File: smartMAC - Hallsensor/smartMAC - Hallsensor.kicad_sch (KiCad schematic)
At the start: 6 parts, among them J1 Conn_01x03_Pin

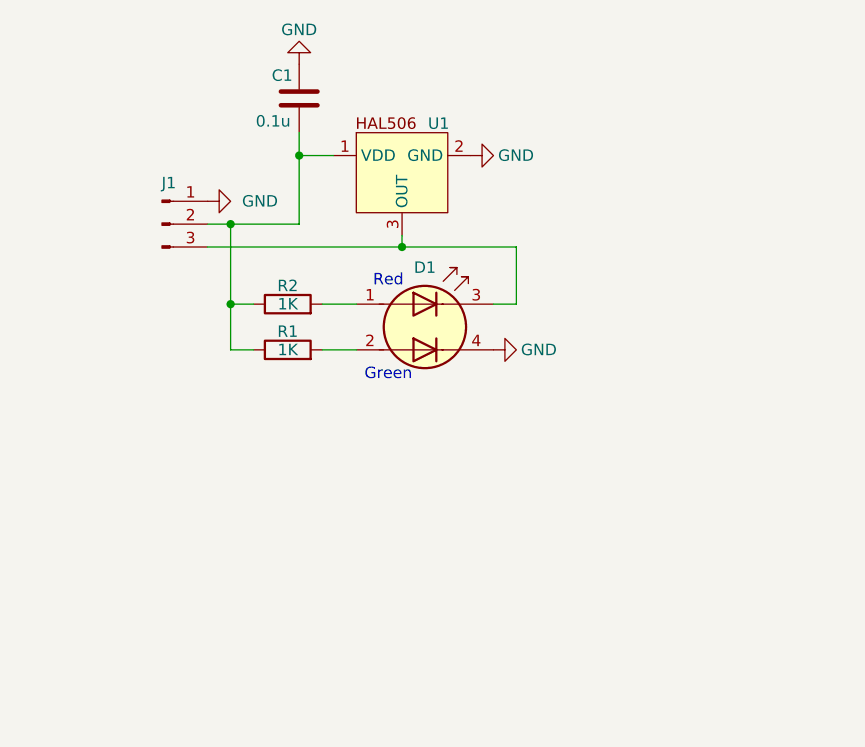
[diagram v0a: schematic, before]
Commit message: Add notes to Lamp Detect and Hallsensor schematics
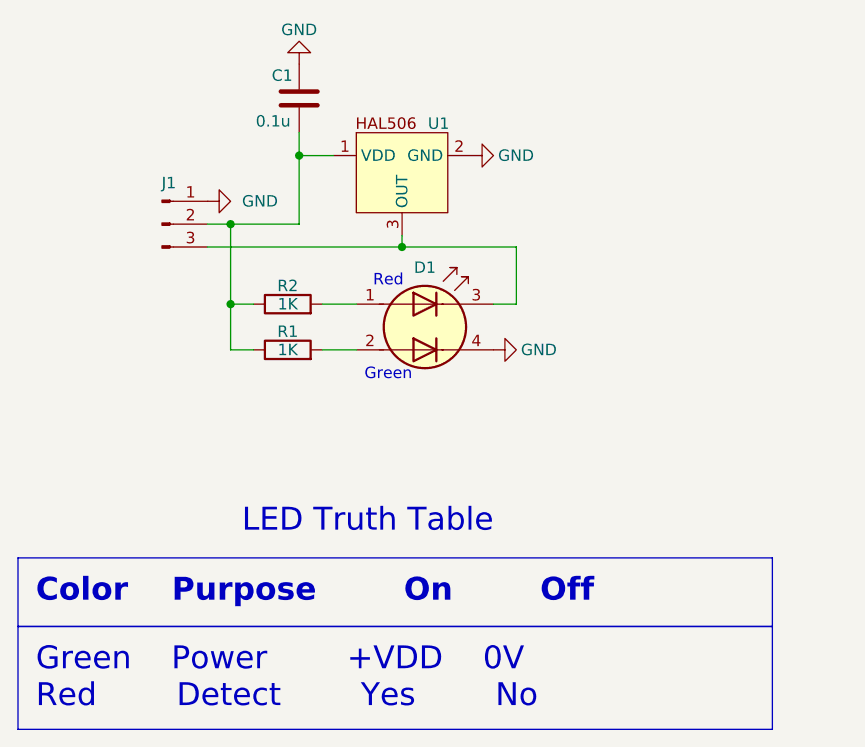
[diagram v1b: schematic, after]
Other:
- note added: "LED Truth Table"
- company: (none) -> Samtronix
- title: (none) -> smartMAC - Hallsensor (62090177-A)
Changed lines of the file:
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@@
 	(generator "eeschema")
 	(generator_version "8.0")
-	(paper "A4")
+	(paper "USLetter")
+	(title_block
+		(title "smartMAC - Hallsensor (62090177-A)")
+		(date "2024-06-19")
+		(rev "1")
+		(company "Samtronix")
+	)
 	(junction
 		(at 110.49 104.14)
@@
 		)
 	)
+	(text_box "Color	Purpose		On		Off"
+		(exclude_from_sim no)
+		(at 86.868 132.334 0)
+		(size 83.82 7.62)
+		(stroke
+			(width 0)
+			(type default)
+		)
+		(fill
+			(type color)
+			(color 0 0 0 0)
+		)
+		(effects
+			(font
+				(size 2.54 2.54)
+				(thickness 0.508)
+				(bold yes)
+			)
+			(justify left top)
+		)
+	)
+	(text_box "Green	Power		+VDD	0V	\nRed		Detect		Yes		No"
+		(exclude_from_sim no)
+		(at 86.868 139.954 0)
+		(size 83.82 11.43)
+		(stroke
+			(width 0)
+			(type default)
+		)
+		(fill
+			(type color)
+			(color 0 0 0 0)
+		)
+		(effects
+			(font
+				(size 2.54 2.54)
+			)
+			(justify left top)
+		)
+	)
 	(text "Red"
 		(exclude_from_sim no)
@@
 			)
 		)
+	)
+	(text "LED Truth Table"
+		(exclude_from_sim no)
+		(at 125.73 128.27 0)
+		(effects
+			(font
+				(size 2.54 2.54)
+			)
+		)
